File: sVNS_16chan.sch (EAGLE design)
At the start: 52 parts, among them IC1 EFM8SB10F8G-A-CSP16R, IC2 OPA990IDCKR, U1 NT3H2211W0FHKH, U2 LT8410EDC-1#TRMPBF, U3 MUX36S16IRSNR, U4 MUX36S16IRSNR

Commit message: Modified sch (unknown change)
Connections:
- removed net IREF: IC2.IN+, R9.2
- net P0.7_IREF: now also IC2.IN+, R9.2
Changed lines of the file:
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@@
 </segment>
 </net>
-<net name="IREF" class="0">
+<net name="P0.7_IREF" class="0">
 <segment>
-<label x="33.02" y="154.94" size="1.778" layer="95"/>
+<label x="27.94" y="154.94" size="1.778" layer="95"/>
 <wire x1="48.26" y1="154.94" x2="40.64" y2="154.94" width="0.1524" layer="91"/>
 <wire x1="40.64" y1="154.94" x2="40.64" y2="157.48" width="0.1524" layer="91"/>

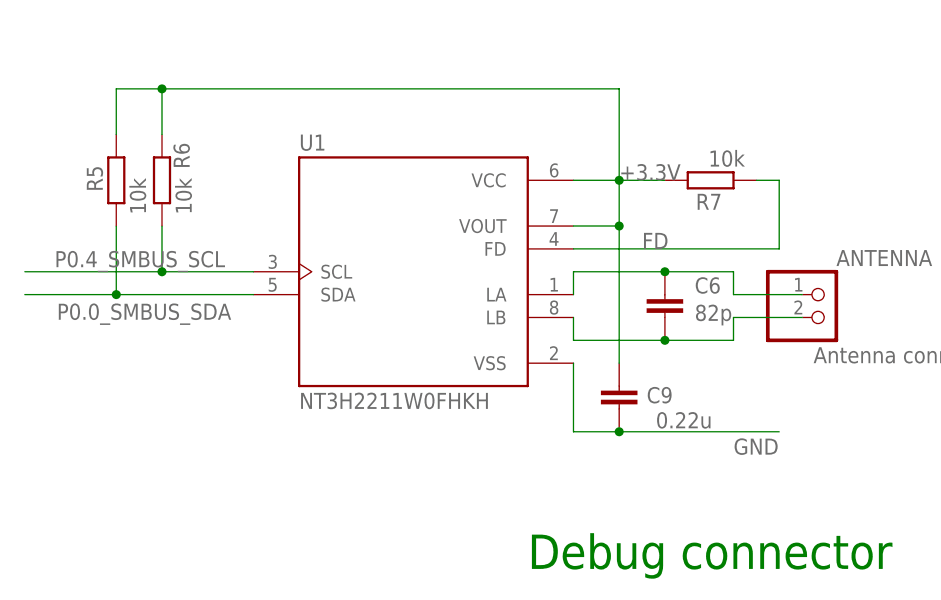
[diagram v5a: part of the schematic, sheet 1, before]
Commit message: Changed MUX36S16 part: removed annoying designator signs. Fixed generated 3.3V voltage check.
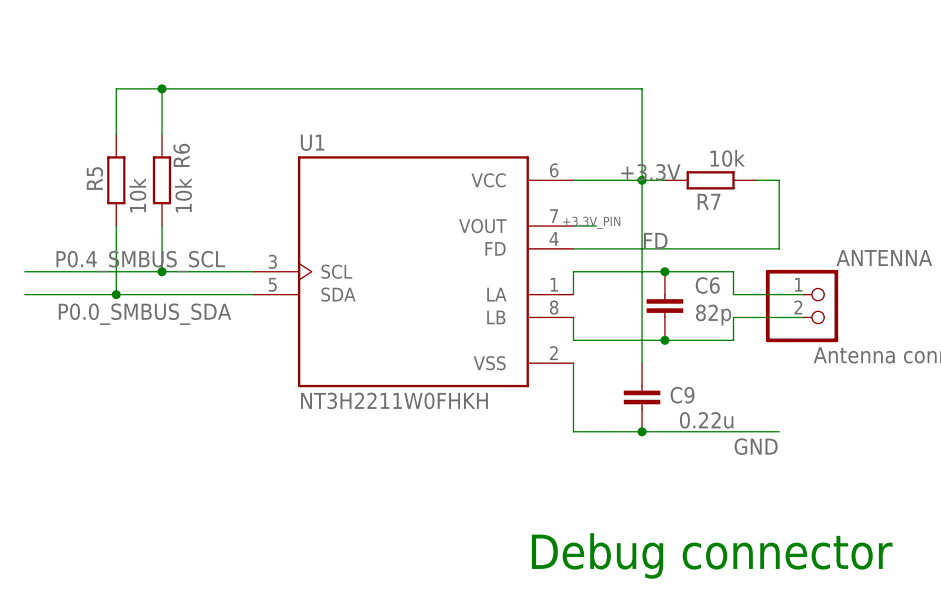
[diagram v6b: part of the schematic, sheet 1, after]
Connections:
- removed net +20V1: C12.1
- removed net GND1: C12.2
- net +3.3V: no longer U1.VOUT
- net +3.3V_PIN: now also U1.VOUT
- net GND: now also C12.2
- net OPAMP_+20V: now also C12.1
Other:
- moved on the sheet: C9
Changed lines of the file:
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@@
 <attribute name="VALUE" x="227.33" y="150.622" size="1.778" layer="96" rot="R180"/>
 </instance>
-<instance part="C9" gate="G$1" x="213.36" y="124.46" smashed="yes">
-<attribute name="NAME" x="216.408" y="122.555" size="1.778" layer="95"/>
-<attribute name="VALUE" x="217.424" y="119.761" size="1.778" layer="96"/>
+<instance part="C9" gate="G$1" x="215.9" y="124.46" smashed="yes">
+<attribute name="NAME" x="218.948" y="122.555" size="1.778" layer="95"/>
+<attribute name="VALUE" x="219.964" y="119.761" size="1.778" layer="96"/>
 </instance>
 <instance part="C7" gate="G$1" x="116.84" y="121.92" smashed="yes" rot="R180">
@@
 <segment>
 <pinref part="C9" gate="G$1" pin="2"/>
-<wire x1="213.36" y1="119.38" x2="208.28" y2="119.38" width="0.1524" layer="91"/>
+<wire x1="215.9" y1="119.38" x2="208.28" y2="119.38" width="0.1524" layer="91"/>
 <pinref part="U1" gate="G$1" pin="VSS"/>
 <wire x1="208.28" y1="119.38" x2="208.28" y2="127" width="0.1524" layer="91"/>
-<wire x1="213.36" y1="119.38" x2="231.14" y2="119.38" width="0.1524" layer="91"/>
-<junction x="213.36" y="119.38"/>
+<wire x1="215.9" y1="119.38" x2="231.14" y2="119.38" width="0.1524" layer="91"/>
+<junction x="215.9" y="119.38"/>
 <label x="226.06" y="116.84" size="1.778" layer="95"/>
 </segment>
@@
 </segment>
 <segment>
-<wire x1="213.36" y1="157.48" x2="162.56" y2="157.48" width="0.1524" layer="91"/>
+<wire x1="215.9" y1="157.48" x2="162.56" y2="157.48" width="0.1524" layer="91"/>
 <wire x1="162.56" y1="152.4" x2="162.56" y2="157.48" width="0.1524" layer="91"/>
 <pinref part="R6" gate="G$1" pin="2"/>
@@
 <wire x1="162.56" y1="157.48" x2="157.48" y2="157.48" width="0.1524" layer="91"/>
 <junction x="162.56" y="157.48"/>
-<pinref part="U1" gate="G$1" pin="VOUT"/>
-<wire x1="208.28" y1="142.24" x2="213.36" y2="142.24" width="0.1524" layer="91"/>
 <pinref part="U1" gate="G$1" pin="VCC"/>
-<wire x1="208.28" y1="147.32" x2="213.36" y2="147.32" width="0.1524" layer="91"/>
+<wire x1="208.28" y1="147.32" x2="215.9" y2="147.32" width="0.1524" layer="91"/>
 <pinref part="R7" gate="G$1" pin="2"/>
-<wire x1="213.36" y1="147.32" x2="218.44" y2="147.32" width="0.1524" layer="91"/>
-<wire x1="213.36" y1="142.24" x2="213.36" y2="147.32" width="0.1524" layer="91"/>
-<junction x="213.36" y="142.24"/>
-<junction x="213.36" y="147.32"/>
-<wire x1="213.36" y1="147.32" x2="213.36" y2="157.48" width="0.1524" layer="91"/>
+<wire x1="215.9" y1="147.32" x2="218.44" y2="147.32" width="0.1524" layer="91"/>
+<junction x="215.9" y="147.32"/>
+<wire x1="215.9" y1="147.32" x2="215.9" y2="157.48" width="0.1524" layer="91"/>
 <pinref part="C9" gate="G$1" pin="1"/>
-<wire x1="213.36" y1="127" x2="213.36" y2="142.24" width="0.1524" layer="91"/>
+<wire x1="215.9" y1="127" x2="215.9" y2="147.32" width="0.1524" layer="91"/>
 <label x="213.36" y="147.32" size="1.778" layer="95"/>
 </segment>
@@
 <wire x1="55.88" y1="27.94" x2="43.18" y2="27.94" width="0.1524" layer="91"/>
 </segment>
+<segment>
+<pinref part="U1" gate="G$1" pin="VOUT"/>
+<wire x1="208.28" y1="142.24" x2="210.82" y2="142.24" width="0.1524" layer="91"/>
+<label x="207.01" y="142.24" size="1.016" layer="95"/>
+</segment>
 </net>
 <net name="+20V_PIN" class="0">
@@
 <junction x="45.72" y="152.4"/>
 <pinref part="IC2" gate="G$1" pin="V-"/>
+<pinref part="C12" gate="G$1" pin="2"/>
 </segment>
 <segment>
@@
 </segment>
 </net>
-<net name="GND1" class="0">
-<segment>
-<pinref part="C12" gate="G$1" pin="2"/>
-<junction x="55.88" y="162.56"/>
-</segment>
-</net>
-<net name="+20V1" class="0">
-<segment>
-<pinref part="C12" gate="G$1" pin="1"/>
-<junction x="63.5" y="162.56"/>
-</segment>
-</net>
 <net name="I_OUT-" class="0">
 <segment>
@@
 <pinref part="IC2" gate="G$1" pin="V+"/>
 <pinref part="R17" gate="G$1" pin="1"/>
-</segment>
-</net>
+<pinref part="C12" gate="G$1" pin="1"/>
+</segment>
+</net>

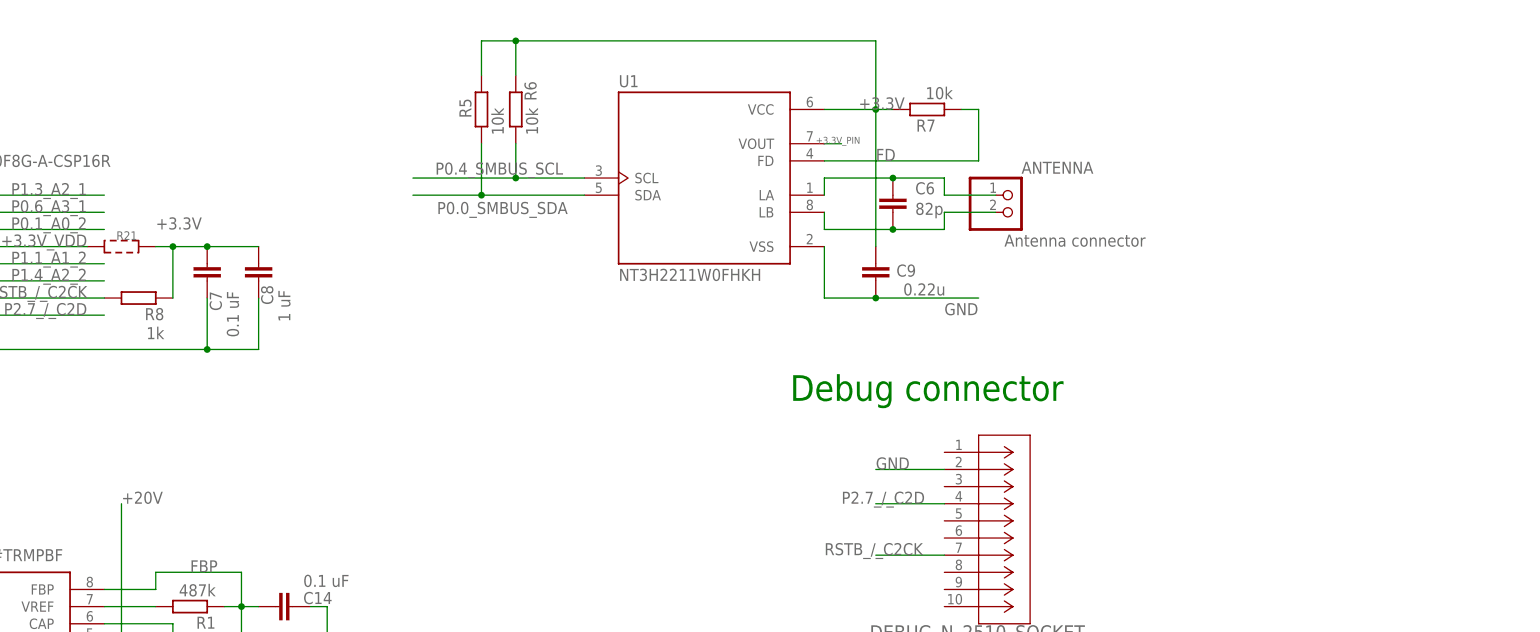
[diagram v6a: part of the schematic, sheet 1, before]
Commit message: Decreased space between components. Changed the antenna connector. Ready for routing
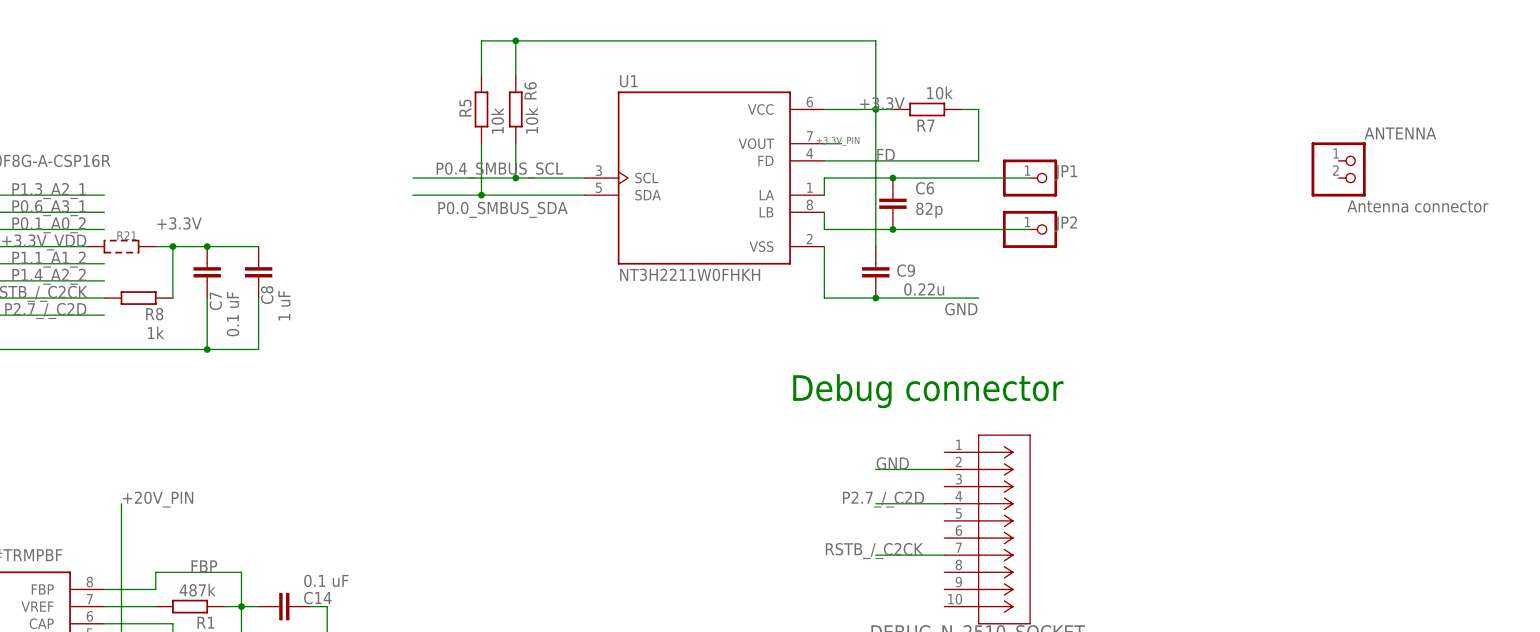
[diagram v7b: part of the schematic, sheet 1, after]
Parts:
- added JP1, JP2: (no value), sVNS_16chan_lib:PINHD-1X1
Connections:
- net +20V: no longer C3.1, U2.VOUT
- net +20V_PIN: now also C3.1, U2.VOUT
- net LA: now also JP1.1; no longer ANTENNA.1
- net LB: now also JP2.1; no longer ANTENNA.2
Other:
- moved on the sheet: ANTENNA
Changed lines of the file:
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@@
 <part name="R24" library="sVNS_16chan_lib" deviceset="SMD_PADS" device="R0402" package3d_urn="urn:adsk.eagle:package:23547/3"/>
 <part name="R25" library="sVNS_16chan_lib" deviceset="SMD_PADS" device="R0402" package3d_urn="urn:adsk.eagle:package:23547/3"/>
+<part name="JP1" library="sVNS_16chan_lib" deviceset="PINHD-1X1" device="" package3d_urn="urn:adsk.eagle:package:22485/2"/>
+<part name="JP2" library="sVNS_16chan_lib" deviceset="PINHD-1X1" device="" package3d_urn="urn:adsk.eagle:package:22485/2"/>
 </parts>
 <sheets>
@@
 <attribute name="VALUE" x="221.742" y="131.699" size="1.778" layer="96"/>
 </instance>
-<instance part="ANTENNA" gate="G$1" x="236.22" y="132.08" smashed="yes">
-<attribute name="NAME" x="237.49" y="137.795" size="1.778" layer="95"/>
-<attribute name="VALUE" x="234.95" y="127" size="1.778" layer="96"/>
+<instance part="ANTENNA" gate="G$1" x="287.02" y="137.16" smashed="yes">
+<attribute name="NAME" x="288.29" y="142.875" size="1.778" layer="95"/>
+<attribute name="VALUE" x="285.75" y="132.08" size="1.778" layer="96"/>
 </instance>
 <instance part="R7" gate="G$1" x="223.52" y="147.32" smashed="yes" rot="R180">
@@
 <attribute name="NAME" x="54.8894" y="22.098" size="1.27" layer="95" rot="R90"/>
 <attribute name="VALUE" x="59.182" y="19.05" size="1.778" layer="96" rot="R90"/>
+</instance>
+<instance part="JP1" gate="G$1" x="241.3" y="137.16" smashed="yes" rot="MR180">
+<attribute name="NAME" x="242.57" y="139.065" size="1.778" layer="95" rot="MR180"/>
+<attribute name="VALUE" x="234.95" y="142.24" size="1.778" layer="96" rot="MR180"/>
+</instance>
+<instance part="JP2" gate="G$1" x="241.3" y="129.54" smashed="yes" rot="MR180">
+<attribute name="NAME" x="242.57" y="131.445" size="1.778" layer="95" rot="MR180"/>
+<attribute name="VALUE" x="234.95" y="134.62" size="1.778" layer="96" rot="MR180"/>
 </instance>
 </instances>
@@
 <wire x1="208.28" y1="137.16" x2="218.44" y2="137.16" width="0.1524" layer="91"/>
 <pinref part="C6" gate="G$1" pin="1"/>
-<wire x1="218.44" y1="137.16" x2="226.06" y2="137.16" width="0.1524" layer="91"/>
 <junction x="218.44" y="137.16"/>
-<pinref part="ANTENNA" gate="G$1" pin="1"/>
-<wire x1="233.68" y1="134.62" x2="226.06" y2="134.62" width="0.1524" layer="91"/>
-<wire x1="226.06" y1="134.62" x2="226.06" y2="137.16" width="0.1524" layer="91"/>
+<pinref part="JP1" gate="G$1" pin="1"/>
+<wire x1="218.44" y1="137.16" x2="238.76" y2="137.16" width="0.1524" layer="91"/>
 </segment>
 </net>
@@
 <wire x1="208.28" y1="129.54" x2="218.44" y2="129.54" width="0.1524" layer="91"/>
 <pinref part="C6" gate="G$1" pin="2"/>
-<wire x1="218.44" y1="129.54" x2="226.06" y2="129.54" width="0.1524" layer="91"/>
 <junction x="218.44" y="129.54"/>
-<pinref part="ANTENNA" gate="G$1" pin="2"/>
-<wire x1="233.68" y1="132.08" x2="226.06" y2="132.08" width="0.1524" layer="91"/>
-<wire x1="226.06" y1="132.08" x2="226.06" y2="129.54" width="0.1524" layer="91"/>
+<pinref part="JP2" gate="G$1" pin="1"/>
+<wire x1="238.76" y1="129.54" x2="218.44" y2="129.54" width="0.1524" layer="91"/>
 </segment>
 </net>
@@
 </segment>
 <segment>
-<pinref part="U2" gate="G$1" pin="VOUT"/>
-<wire x1="101.6" y1="68.58" x2="104.14" y2="68.58" width="0.1524" layer="91"/>
-<wire x1="104.14" y1="68.58" x2="104.14" y2="50.8" width="0.1524" layer="91"/>
-<pinref part="C3" gate="G$1" pin="1"/>
-<wire x1="104.14" y1="50.8" x2="109.22" y2="50.8" width="0.1524" layer="91"/>
-<wire x1="104.14" y1="68.58" x2="104.14" y2="88.9" width="0.1524" layer="91"/>
-<junction x="104.14" y="68.58"/>
-<label x="104.14" y="88.9" size="1.778" layer="95"/>
-</segment>
-<segment>
 <wire x1="30.48" y1="17.78" x2="20.32" y2="17.78" width="0.1524" layer="91"/>
 <label x="25.4" y="17.78" size="1.778" layer="95" rot="MR0"/>
@@
 <pinref part="R24" gate="G$1" pin="2"/>
 </segment>
-</net>
+<segment>
+<pinref part="U2" gate="G$1" pin="VOUT"/>
+<wire x1="101.6" y1="68.58" x2="104.14" y2="68.58" width="0.1524" layer="91"/>
+<wire x1="104.14" y1="68.58" x2="104.14" y2="50.8" width="0.1524" layer="91"/>
+<pinref part="C3" gate="G$1" pin="1"/>
+<wire x1="104.14" y1="50.8" x2="109.22" y2="50.8" width="0.1524" layer="91"/>
+<wire x1="104.14" y1="68.58" x2="104.14" y2="88.9" width="0.1524" layer="91"/>
+<junction x="104.14" y="68.58"/>
+<label x="104.14" y="88.9" size="1.778" layer="95"/>
+</segment>
+</net>

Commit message: Experimentation and routing
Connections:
- net +3.3V: no longer C7.2, C8.1, R8.1
- net +3.3V_VDD: now also C7.2, C8.1, R8.1
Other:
- moved on the sheet: R21
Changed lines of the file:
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@@
 <part name="R19" library="sVNS_16chan_lib" deviceset="SMD_PADS" device="R0402" package3d_urn="urn:adsk.eagle:package:23547/3"/>
 <part name="R20" library="sVNS_16chan_lib" deviceset="SMD_PADS" device="R0402" package3d_urn="urn:adsk.eagle:package:23547/3"/>
-<part name="R21" library="sVNS_16chan_lib" deviceset="SMD_PADS" device="R0402" package3d_urn="urn:adsk.eagle:package:23547/3"/>
 <part name="R22" library="sVNS_16chan_lib" deviceset="SMD_PADS" device="R0402" package3d_urn="urn:adsk.eagle:package:23547/3"/>
 <part name="R23" library="sVNS_16chan_lib" deviceset="SMD_PADS" device="R0402" package3d_urn="urn:adsk.eagle:package:23547/3"/>
@@
 <part name="JP1" library="sVNS_16chan_lib" deviceset="PINHD-1X1" device="" package3d_urn="urn:adsk.eagle:package:22485/2"/>
 <part name="JP2" library="sVNS_16chan_lib" deviceset="PINHD-1X1" device="" package3d_urn="urn:adsk.eagle:package:22485/2"/>
+<part name="R21" library="sVNS_16chan_lib" deviceset="SMD_PADS" device="R0402" package3d_urn="urn:adsk.eagle:package:23547/3"/>
 </parts>
 <sheets>
@@
 <attribute name="VALUE" x="131.064" y="76.581" size="1.778" layer="96"/>
 </instance>
-<instance part="R21" gate="G$1" x="104.14" y="127" smashed="yes">
-<attribute name="NAME" x="103.378" y="127.9906" size="1.27" layer="95"/>
-<attribute name="VALUE" x="100.33" y="123.698" size="1.778" layer="96"/>
-</instance>
 <instance part="R22" gate="G$1" x="20.32" y="134.62" smashed="yes">
 <attribute name="NAME" x="19.558" y="135.6106" size="1.27" layer="95"/>
@@
 <attribute name="NAME" x="242.57" y="131.445" size="1.778" layer="95" rot="MR180"/>
 <attribute name="VALUE" x="234.95" y="134.62" size="1.778" layer="96" rot="MR180"/>
+</instance>
+<instance part="R21" gate="G$1" x="124.46" y="137.16" smashed="yes" rot="R90">
+<attribute name="NAME" x="123.4694" y="136.398" size="1.27" layer="95" rot="R90"/>
+<attribute name="VALUE" x="127.762" y="133.35" size="1.778" layer="96" rot="R90"/>
 </instance>
 </instances>
@@
 </segment>
 <segment>
-<pinref part="C8" gate="G$1" pin="1"/>
-<wire x1="124.46" y1="127" x2="116.84" y2="127" width="0.1524" layer="91"/>
-<pinref part="C7" gate="G$1" pin="2"/>
-<junction x="116.84" y="127"/>
-<wire x1="116.84" y1="127" x2="111.76" y2="127" width="0.1524" layer="91"/>
-<pinref part="R8" gate="G$1" pin="1"/>
-<wire x1="111.76" y1="119.38" x2="111.76" y2="127" width="0.1524" layer="91"/>
-<junction x="111.76" y="127"/>
-<wire x1="111.76" y1="127" x2="109.22" y2="127" width="0.1524" layer="91"/>
-<label x="109.22" y="129.54" size="1.778" layer="95"/>
-<pinref part="R21" gate="G$1" pin="2"/>
-</segment>
-<segment>
 <junction x="58.42" y="73.66"/>
 <wire x1="58.42" y1="73.66" x2="58.42" y2="88.9" width="0.1524" layer="91"/>
@@
 <wire x1="58.42" y1="73.66" x2="55.88" y2="73.66" width="0.1524" layer="91"/>
 <pinref part="R23" gate="G$1" pin="2"/>
+</segment>
+<segment>
+<pinref part="R21" gate="G$1" pin="2"/>
+<wire x1="124.46" y1="142.24" x2="124.46" y2="147.32" width="0.1524" layer="91"/>
+<label x="121.92" y="147.32" size="1.778" layer="95"/>
 </segment>
 </net>
@@
 <net name="+3.3V_VDD" class="0">
 <segment>
+<pinref part="C7" gate="G$1" pin="2"/>
+<wire x1="116.84" y1="127" x2="111.76" y2="127" width="0.1524" layer="91"/>
+<pinref part="R8" gate="G$1" pin="1"/>
+<wire x1="111.76" y1="119.38" x2="111.76" y2="127" width="0.1524" layer="91"/>
+<junction x="111.76" y="127"/>
+<label x="109.22" y="129.54" size="1.778" layer="95"/>
 <pinref part="IC1" gate="G$1" pin="VDD"/>
 <label x="99.06" y="127" size="1.778" layer="95" align="bottom-right"/>
-<wire x1="99.06" y1="127" x2="78.74" y2="127" width="0.1524" layer="91"/>
+<wire x1="111.76" y1="127" x2="78.74" y2="127" width="0.1524" layer="91"/>
+<pinref part="C8" gate="G$1" pin="1"/>
 <pinref part="R21" gate="G$1" pin="1"/>
-</segment>
-</net>
+<wire x1="124.46" y1="132.08" x2="124.46" y2="127" width="0.1524" layer="91"/>
+<wire x1="124.46" y1="127" x2="116.84" y2="127" width="0.1524" layer="91"/>
+<junction x="124.46" y="127"/>
+<junction x="116.84" y="127"/>
+</segment>
+</net>
